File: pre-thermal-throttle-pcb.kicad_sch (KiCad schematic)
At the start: 21 parts, among them P1 Header 4, U1 CRE1S1205SC, U2 SN65HVD230, U3 MCP3008, U4 ESP32-DevKitC, U5 BMI088

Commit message: Label stuff
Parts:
- C1, C2: symbol pspice:CAP -> Device:C
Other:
- note added: "CAN"
- note added: "IMU"
- note added: "Steering Wheel + RS485 Transceiver"
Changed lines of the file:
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@@
   (junction (at 388.62 149.86) (diameter 0) (color 0 0 0 0)
   )
+  (wire (pts (xy 562.61 285.75) (xy 566.42 285.75))
+    (stroke (width 0) (type default) (color 0 0 0 0))
+  )
+  (polyline (pts (xy 345.44 87.63) (xy 490.22 87.63))
+    (stroke (width 0) (type default) (color 0 0 0 0))
+  )
   (wire (pts (xy 549.91 270.51) (xy 561.34 270.51))
     (stroke (width 0) (type default) (color 0 0 0 0))
   )
+  (wire (pts (xy 574.04 283.21) (xy 575.31 283.21))
+    (stroke (width 0) (type default) (color 0 0 0 0))
+  )
   (wire (pts (xy 549.91 283.21) (xy 557.53 283.21))
     (stroke (width 0) (type default) (color 0 0 0 0))
@@
     (stroke (width 0) (type default) (color 0 0 0 0))
   )
+  (polyline (pts (xy 345.44 87.63) (xy 345.44 175.26))
+    (stroke (width 0) (type default) (color 0 0 0 0))
+  )
   (wire (pts (xy 430.53 129.54) (xy 436.88 129.54))
     (stroke (width 0) (type default) (color 0 0 0 0))
@@
     (stroke (width 0) (type default) (color 0 0 0 0))
   )
+  (polyline (pts (xy 336.55 100.33) (xy 336.55 163.83))
+    (stroke (width 0) (type default) (color 0 0 0 0))
+  )
+  (polyline (pts (xy 233.68 100.33) (xy 233.68 163.83))
+    (stroke (width 0) (type default) (color 0 0 0 0))
+  )
+  (polyline (pts (xy 490.22 87.63) (xy 490.22 175.26))
+    (stroke (width 0) (type default) (color 0 0 0 0))
+  )
   (wire (pts (xy 514.35 288.29) (xy 511.81 288.29))
     (stroke (width 0) (type default) (color 0 0 0 0))
   )
+  (polyline (pts (xy 387.35 266.7) (xy 387.35 328.93))
+    (stroke (width 0) (type default) (color 0 0 0 0))
+  )
   (wire (pts (xy 252.73 213.36) (xy 252.73 215.9))
     (stroke (width 0) (type default) (color 0 0 0 0))
@@
     (stroke (width 0) (type default) (color 0 0 0 0))
   )
-  (wire (pts (xy 557.53 285.75) (xy 557.53 288.29))
+  (polyline (pts (xy 588.01 316.23) (xy 492.76 316.23))
+    (stroke (width 0) (type default) (color 0 0 0 0))
+  )
+  (wire (pts (xy 557.53 285.75) (xy 557.53 290.83))
     (stroke (width 0) (type default) (color 0 0 0 0))
   )
@@
     (stroke (width 0) (type default) (color 0 0 0 0))
   )
+  (polyline (pts (xy 292.1 266.7) (xy 387.35 266.7))
+    (stroke (width 0) (type default) (color 0 0 0 0))
+  )
+  (polyline (pts (xy 292.1 265.43) (xy 292.1 328.93))
+    (stroke (width 0) (type default) (color 0 0 0 0))
+  )
   (wire (pts (xy 317.5 294.64) (xy 307.34 294.64))
     (stroke (width 0) (type default) (color 0 0 0 0))
@@
     (stroke (width 0) (type default) (color 0 0 0 0))
   )
+  (polyline (pts (xy 588.01 252.73) (xy 588.01 316.23))
+    (stroke (width 0) (type default) (color 0 0 0 0))
+  )
   (wire (pts (xy 561.34 270.51) (xy 561.34 275.59))
     (stroke (width 0) (type default) (color 0 0 0 0))
@@
     (stroke (width 0) (type default) (color 0 0 0 0))
   )
+  (wire (pts (xy 561.34 275.59) (xy 563.88 275.59))
+    (stroke (width 0) (type default) (color 0 0 0 0))
+  )
   (wire (pts (xy 388.62 149.86) (xy 415.29 149.86))
     (stroke (width 0) (type default) (color 0 0 0 0))
@@
     (stroke (width 0) (type default) (color 0 0 0 0))
   )
+  (polyline (pts (xy 492.76 252.73) (xy 588.01 252.73))
+    (stroke (width 0) (type default) (color 0 0 0 0))
+  )
   (wire (pts (xy 551.18 278.13) (xy 551.18 280.67))
     (stroke (width 0) (type default) (color 0 0 0 0))
@@
     (stroke (width 0) (type default) (color 0 0 0 0))
   )
+  (wire (pts (xy 574.04 285.75) (xy 574.04 283.21))
+    (stroke (width 0) (type default) (color 0 0 0 0))
+  )
+  (polyline (pts (xy 233.68 100.33) (xy 336.55 100.33))
+    (stroke (width 0) (type default) (color 0 0 0 0))
+  )
   (wire (pts (xy 514.35 300.99) (xy 511.81 300.99))
     (stroke (width 0) (type default) (color 0 0 0 0))
@@
     (stroke (width 0) (type default) (color 0 0 0 0))
   )
+  (polyline (pts (xy 336.55 163.83) (xy 233.68 163.83))
+    (stroke (width 0) (type default) (color 0 0 0 0))
+  )
   (wire (pts (xy 368.3 149.86) (xy 368.3 132.08))
     (stroke (width 0) (type default) (color 0 0 0 0))
   )
+  (polyline (pts (xy 492.76 252.73) (xy 492.76 316.23))
+    (stroke (width 0) (type default) (color 0 0 0 0))
+  )
   (wire (pts (xy 345.44 299.72) (xy 345.44 302.26))
     (stroke (width 0) (type default) (color 0 0 0 0))
@@
     (stroke (width 0) (type default) (color 0 0 0 0))
   )
+  (wire (pts (xy 571.5 275.59) (xy 574.04 275.59))
+    (stroke (width 0) (type default) (color 0 0 0 0))
+  )
   (wire (pts (xy 363.22 149.86) (xy 368.3 149.86))
     (stroke (width 0) (type default) (color 0 0 0 0))
@@
     (stroke (width 0) (type default) (color 0 0 0 0))
   )
+  (polyline (pts (xy 490.22 175.26) (xy 345.44 175.26))
+    (stroke (width 0) (type default) (color 0 0 0 0))
+  )
   (wire (pts (xy 359.41 294.64) (xy 359.41 297.18))
     (stroke (width 0) (type default) (color 0 0 0 0))
@@
     (stroke (width 0) (type default) (color 0 0 0 0))
   )
-  (wire (pts (xy 562.61 278.13) (xy 562.61 283.21))
-    (stroke (width 0) (type default) (color 0 0 0 0))
+  (polyline (pts (xy 387.35 328.93) (xy 292.1 328.93))
+    (stroke (width 0) (type default) (color 0 0 0 0))
+  )
+  (wire (pts (xy 562.61 278.13) (xy 562.61 285.75))
+    (stroke (width 0) (type default) (color 0 0 0 0))
+  )
+  (text "IMU" (at 532.13 261.62 0)
+    (effects (font (size 3 3)) (justify left bottom))
   )
   (text "ADC" (at 444.5 114.3 0)
     (effects (font (size 5 5)) (justify left bottom))
   )
+  (text "Steering Wheel + RS485 Transceiver" (at 243.84 107.95 0)
+    (effects (font (size 3 3)) (justify left bottom))
+  )
   (text "some gpio pin" (at 474.98 220.98 0)
     (effects (font (size 1.27 1.27)) (justify left bottom))
+  )
+  (text "CAN" (at 330.2 278.13 0)
+    (effects (font (size 3 3)) (justify left bottom))
   )
   (text "Motor Thermistor Measurements" (at 351.79 97.79 0)
@@
     )
   )
-  (global_label "ESP MISO" (shape input) (at 557.53 288.29 0) (fields_autoplaced)
+  (global_label "ESP MISO" (shape input) (at 557.53 290.83 0) (fields_autoplaced)
     (effects (font (size 1.27 1.27)) (justify left))
-    (property "Intersheet References" "${INTERSHEET_REFS}" (id 0) (at 569.1355 288.2106 0)
+    (property "Intersheet References" "${INTERSHEET_REFS}" (id 0) (at 569.1355 290.7506 0)
       (effects (font (size 1.27 1.27)) (justify left) hide)
     )
@@
     (pin "2")
   )
-  (symbol (lib_id "pspice:CAP") (at 568.96 283.21 90) (unit 1)
-    (in_bom yes) (on_board yes) (fields_autoplaced)
-    (property "Reference" "C2" (id 0) (at 568.96 274.32 90))
-    (property "Value" "100 nF" (id 1) (at 568.96 276.86 90))
-    (property "Footprint" "" (id 2) (at 568.96 283.21 0)
-      (effects (font (size 1.27 1.27)) hide)
-    )
-    (property "Datasheet" "~" (id 3) (at 568.96 283.21 0)
+  (symbol (lib_id "Device:C") (at 570.23 285.75 90) (unit 1)
+    (in_bom yes) (on_board yes)
+    (property "Reference" "C2" (id 0) (at 570.23 279.4 90))
+    (property "Value" "100 nF" (id 1) (at 570.23 281.94 90))
+    (property "Footprint" "" (id 2) (at 574.04 284.7848 0)
+      (effects (font (size 1.27 1.27)) hide)
+    )
+    (property "Datasheet" "~" (id 3) (at 570.23 285.75 0)
       (effects (font (size 1.27 1.27)) hide)
     )
@@
     (pin "1")
   )
-  (symbol (lib_id "pspice:CAP") (at 567.69 275.59 90) (unit 1)
-    (in_bom yes) (on_board yes) (fields_autoplaced)
-    (property "Reference" "C1" (id 0) (at 567.69 266.7 90))
-    (property "Value" "100 nF" (id 1) (at 567.69 269.24 90))
-    (property "Footprint" "" (id 2) (at 567.69 275.59 0)
-      (effects (font (size 1.27 1.27)) hide)
-    )
+  (symbol (lib_id "Device:C") (at 567.69 275.59 90) (unit 1)
+    (in_bom yes) (on_board yes)
+    (property "Reference" "C1" (id 0) (at 567.69 269.24 90))
+    (property "Value" "100 nF" (id 1) (at 567.69 271.78 90))
+    (property "Footprint" "" (id 2) (at 571.5 274.6248 0)
+      (effects (font (size 1.27 1.27)) hide)
+    )

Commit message: Add switching regulator circuit basic schematic, values need compute
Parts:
- removed P1: Header 4, symbol Connector:Conn_01x04_Female
- removed U1: CRE1S1205SC, Converter_DCDC:Converter_DCDC_Murata_CRE1xxxxxxSC_THT, symbol Regulator_Switching:CRE1S1205SC
- added CREG3, CREG5, CREGin: C, symbol Device:C
- added CREGout: C_Polarized, symbol Device:C_Polarized
- added DREG1: D, symbol Device:D
- added IC1: A7986ATR, SOIC127P600X175-9N, symbol A7986ATR:A7986ATR
- added J2: Motor Throttle Connector, Connector_JST:JST_PH_B2B-PH-K_1x02_P2.00mm_Vertical, symbol Connector:Conn_01x02_Female
- added LREG1: L, symbol Device:L
- added R7: 1M, Resistor_SMD:R_0805_2012Metric, symbol Device:R
- added RREG1, RREG2, RREG3: R, symbol Device:R
- gave numbers to parts that had none: 10
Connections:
- net ESP MISO is gone; now on net ESP CIPO: U5.10 (SDO2), U5.15 (SDO1)
- net ESP MOSI is gone; now on net ESP COPI: U5.9 (SDA/SDI)
- net +12V: now also CREGin.1, IC1.3 (EN), IC1.8 (VCC)
- net +3.3V: now also U2.3 (VCC), U3.16 (Vdd), U4.1 (3V3), CREGout.1, LREG1.2, RREG1.2
- net +5V: now also U3.15 (Vref), U4.19 (5V)
- net ESP Accel : now also U4.33 (GPIO21)
- net ESP Gyro CS: now also U4.36 (GPIO22)
- net ESP SPI CLK: now also U3.13 (CLK), U4.30 (GPIO18)
- net GND: now also U2.2 (GND), U3.14 (AGND), U3.9 (DGND), U4.14 (GND), U4.32 (GND), U4.38 (GND), CREGin.2, CREGout.2, DREG1.2 (A), IC1.7 (GND), J2.2 (Pin_2), R7.2, RREG2.1
- net CAN_RXD: now reaches U4.10 (DAC_2/ADC2_CH9/GPIO26)
- net CAN_RXD: now also U2.4 (R)
- net ESP CIPO: now reaches U4.31 (GPIO19)
- net ESP CIPO: now also U3.12 (Dout)
- net ESP COPI: now reaches U4.37 (GPIO23)
- net ESP COPI: now also U3.11 (Din)
- net ESP ADC CS: now reaches U4.4 (SENSOR_VN/GPIO39/ADC1_CH3)
- net ESP ADC CS: now also U3.10 (~{CS}/SHDN)
- net CAN_TXD: now reaches U4.9 (DAC_1/ADC2_CH8/GPIO25)
- net CAN_TXD: now also U2.1 (D)
- net at R1.1, U2.8 (Rs): no longer U2.2 (GND)
- net THROTTLE_SIG: now reaches U3.5 (CH4)
- net THROTTLE_SIG: now also J2.1 (Pin_1), R7.1
- new net: CREG3.1, RREG3.2
- new net: CREG3.2, CREG5.1, IC1.5 (FB), RREG1.1, RREG2.2
- new net: CREG5.2, IC1.4 (COMP), RREG3.1
- new net: DREG1.1 (K), IC1.1 (OUT), LREG1.1
- no-connect marks 0 -> 4
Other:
- note added: "12V-3.3V Switching Regulator"
- note added: "5V Reference (For thermistor ONLY)"
- moved on the sheet: C1, C2, U5

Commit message: Setup footprints and add bypass caps
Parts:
- removed can1: Header 2, symbol Connector:Conn_01x02_Female
- added C1, C10, C11, C12, C13, C2, C3, C4, C5, C8, C9: 100 nF, Capacitor_SMD:C_0805_2012Metric, symbol Device:C
- added J1: RJHSE-5381-ND, Connector_RJ:RJ45_Amphenol_RJHSE538X, symbol Connector:RJ45_LED_Shielded
- added R3, R5: 130R, Resistor_SMD:R_0805_2012Metric, symbol Device:R_US
- added R4: 10K, Resistor_SMD:R_0805_2012Metric, symbol Device:R_US
- added R6: 120R, Resistor_THT:R_Axial_DIN0309_L9.0mm_D3.2mm_P15.24mm_Horizontal, symbol Device:R_US
- C6: renamed from C1; footprint (none) -> Capacitor_SMD:C_0805_2012Metric
- C7: renamed from C2; footprint (none) -> Capacitor_SMD:C_0805_2012Metric
- CREG3, CREG5: footprint (none) -> Capacitor_SMD:C_0805_2012Metric
- CREGin1: renamed from CREGin; footprint (none) -> Capacitor_SMD:C_0805_2012Metric
- CREGout1: renamed from CREGout; footprint (none) -> Capacitor_THT:CP_Radial_D8.0mm_P3.80mm
- DREG1: footprint (none) -> Diode_SMD:D_0805_2012Metric
- LREG1: footprint (none) -> Inductor_SMD:L_Taiyo-Yuden_NR-80xx_HandSoldering
- R1, RREG1, RREG2, RREG3: footprint (none) -> Resistor_SMD:R_0805_2012Metric
- R2: value 120 -> 120R; footprint (none) -> Resistor_THT:R_Axial_DIN0309_L9.0mm_D3.2mm_P15.24mm_Horizontal
- TH1, TH2, TH3, TH4: footprint (none) -> Connector_JST:JST_PH_B2B-PH-K_1x02_P2.00mm_Vertical
- U3: renamed from U6; value MAX3485 -> MAX3485CSA; footprint (none) -> Package_SO:SOIC-8-1EP_3.9x4.9mm_P1.27mm_EP2.41x3.81mm_ThermalVias
- U4: renamed from U3; footprint (none) -> Package_DIP:DIP-16_W7.62mm
- renumbered J1 to J2, J2 to J3, R6 to R10, R7 to R11, R3 to R7, R4 to R8, R5 to R9, U2 to U1, U5 to U2, U4 to U5
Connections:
- net +12V: now also C4.1, C5.1, J1.4, J1.5
- net +3.3V: now also C1.1, C11.1, C13.1, C3.2, J1.12
- net +5V: now also C10.1, C12.1, C8.1, C9.1
- net GND: now also C1.2, C10.2, C11.2, C12.2, C13.2, C2.1, C3.1, C4.2, C5.2, C8.2, C9.2, J1.7, J1.8, R3.1, R4.2, R5.1
- net RS485 RTS: now also U5.5 (VDET_1/GPIO34/ADC1_CH6)
- net STEERING_A: now also R6.2
- net STEERING_B: now also R6.1
- net CAR_CANH: now reaches R2.1, U1.7 (CANH)
- net CAR_CANH: now also J1.1
- net CAR_CANL: now reaches R2.2, U1.6 (CANL)
- net CAR_CANL: now also J1.2
- net ESP_OK_LED: now reaches U5.3 (SENSOR_VP/GPIO36/ADC1_CH0)
- net ESP_OK_LED: now also C2.2, J1.10, R4.1
- new net: J1.11, R3.2
- new net: J1.9, R5.2
- no-connect marks 4 -> 5
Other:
- note added: "Car-wide connection"
- note added: "GREEN"
- note added: "Power layout follows POE standard mode B LEDs are yellow, green at 2V, 10mA"
- note added: "YELLOW"
- note removed: "some gpio pin"
- moved on the sheet: C6, C7, CREG3, CREG5, CREGin1, CREGout1, DREG1, IC1, J2, J3, LREG1, R1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

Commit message: Finish part selection
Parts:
- removed CREG3, CREG5: C, Capacitor_SMD:C_0805_2012Metric, symbol Device:C
- removed CREGout1: C_Polarized, Capacitor_THT:CP_Radial_D8.0mm_P3.80mm, symbol Device:C_Polarized
- removed DREG1: D, Diode_SMD:D_0805_2012Metric, symbol Device:D
- removed IC1: A7986ATR, SOIC127P600X175-9N, symbol A7986ATR:A7986ATR
- removed RREG1, RREG2, RREG3: R, Resistor_SMD:R_0805_2012Metric, symbol Device:R
- added C14, C15, C16, C17, C18, C19, C20, C21: 100 nF, Capacitor_SMD:C_0805_2012Metric, symbol Device:C
- added CREGboot1, CREGinx1: 100nF, Capacitor_SMD:C_0805_2012Metric, symbol Device:C
- added CREGin2, CREGin3: 1uF, Capacitor_SMD:C_0805_2012Metric, symbol Device:C
- added CREGout1: 47uF, Capacitor_SMD:C_0805_2012Metric, symbol Device:C
- added H1, H2, H3, H4: MountingHole_Pad, MountingHole:MountingHole_3mm_Pad_Via, symbol Mechanical:MountingHole_Pad
- added IC1: LMR51420XFDDCR, SOT95P280X110-6N, symbol LMR51420XFDDCR:LMR51420XFDDCR
- added IC2, IC3, IC4, IC5: ADR02BRZ-REEL7, ADR02BRZ:SOIC127P600X175-8N, symbol ADR02BRZ-REEL7:ADR02BRZ-REEL7
- added RREGfbb1: 22.1k, Resistor_SMD:R_0805_2012Metric, symbol Device:R_US
- added RREGfbt1: 100k, Resistor_SMD:R_0805_2012Metric, symbol Device:R_US
- CREGin1: value C -> 1uF
- J2: footprint Connector_JST:JST_PH_B4B-PH-K_1x04_P2.00mm_Vertical -> Connector_JST:JST_XH_B4B-XH-A_1x04_P2.50mm_Vertical
- J3, TH1, TH2, TH3, TH4: footprint Connector_JST:JST_PH_B2B-PH-K_1x02_P2.00mm_Vertical -> Connector_JST:JST_XH_B2B-XH-A_1x02_P2.50mm_Vertical
- LREG1: value L -> 6uH SRP1265A-6R0M; footprint Inductor_SMD:L_Taiyo-Yuden_NR-80xx_HandSoldering -> libraries:L_Bourns_SRP1260A
- U2: footprint PQFN50P450X300X100-16N -> bmi088:PQFN50P450X300X100-16N
- U3: footprint Package_SO:SOIC-8-1EP_3.9x4.9mm_P1.27mm_EP2.41x3.81mm_ThermalVias -> libraries:SOIC-8-1EP_3.9x4.9mm_P1.27mm_EP2.41x3.81mm_ThermalVias
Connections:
- net +12V: now also C14.2, C15.2, C16.2, C17.2, CREGin2.1, CREGin3.1, CREGinx1.1, IC1.3 (VIN), IC1.5 (EN), IC2.2 (VIN), IC3.2 (VIN), IC4.2 (VIN), IC5.2 (VIN)
- net +3.3V: now also CREGout1.1, RREGfbt1.1
- net +5V: no longer TH1.1, TH2.1, TH3.1, TH4.1
- net GND: now also C14.1, C15.1, C16.1, C17.1, C18.1, C19.1, C20.1, C21.1, CREGin2.2, CREGin3.2, CREGinx1.2, CREGout1.2, H1.1, H2.1, H3.1, H4.1, IC1.1 (GND), IC2.4 (GND), IC3.4 (GND), IC4.4 (GND), IC5.4 (GND), RREGfbb1.2
- net ADC_CH0: now reaches R7.1, U4.1 (CH0)
- net ADC_CH0: now also TH1.1; no longer TH1.2
- net ADC_CH2: now reaches R8.1, U4.3 (CH2)
- net ADC_CH2: now also TH2.1; no longer TH2.2
- net ADC_CH1: now reaches R9.1, U4.2 (CH1)
- net ADC_CH1: now also TH3.1; no longer TH3.2
- net at LREG1.1: now also CREGboot1.2, IC1.2 (SW)
- new net: CREGboot1.1, IC1.6 (CB)
- new net: C18.2, IC2.6 (VOUT), TH1.2
- new net: C21.2, IC5.6 (VOUT), TH4.2
- new net: C20.2, IC4.6 (VOUT), TH3.2
- new net: IC1.4 (FB), RREGfbb1.1, RREGfbt1.2
- new net: C19.2, IC3.6 (VOUT), TH2.2
- new net ADC_CH3: U4.4 (CH3)
- new net ADC_CH4: R10.1, TH4.1
- no-connect marks 5 -> 22
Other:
- note added: "ESP32"
- note removed: "5V Reference (For thermistor ONLY)"
- moved on the sheet: C10, C11, C12, C13, C2, C3, C4, C5, C6, C7, C8, C9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

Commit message: Add extra rj45 for CAN splice and connect imu ints
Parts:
- added C22, C23, C24, C25: 100 nF, Capacitor_SMD:C_0805_2012Metric, symbol Device:C
- added J4: RJHSE-5381-ND, Connector_RJ:RJ45_Amphenol_RJHSE538X, symbol Connector:RJ45_LED_Shielded
- added R12, R14: 130R, Resistor_SMD:R_0805_2012Metric, symbol Device:R_US
- added R13: 10K, Resistor_SMD:R_0805_2012Metric, symbol Device:R_US
- IC1: footprint SOT95P280X110-6N -> LMR51420XFDDCR:SOT95P280X110-6N
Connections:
- net +12V: now also C24.1, C25.1, J4.4, J4.5
- net +3.3V: now also C23.2, J4.12
- net CAR_CANH: now also J4.1
- net CAR_CANL: now also J4.2
- net ESP_OK_LED: now also C22.2, J4.10, R13.1
- net GND: now also C22.1, C23.1, C24.2, C25.2, J4.7, J4.8, R12.1, R13.2, R14.1
- net IMU_INT1: now reaches U5.21 (SD_DATA0/GPIO7)
- net IMU_INT1: now also U2.16 (INT1)
- net IMU_INT2: now reaches U5.22 (SD_DATA1/GPIO8)
- net IMU_INT2: now also U2.13 (INT4)
- new net: J4.11, R12.2
- new net: J4.9, R14.2
- no-connect marks 22 -> 23

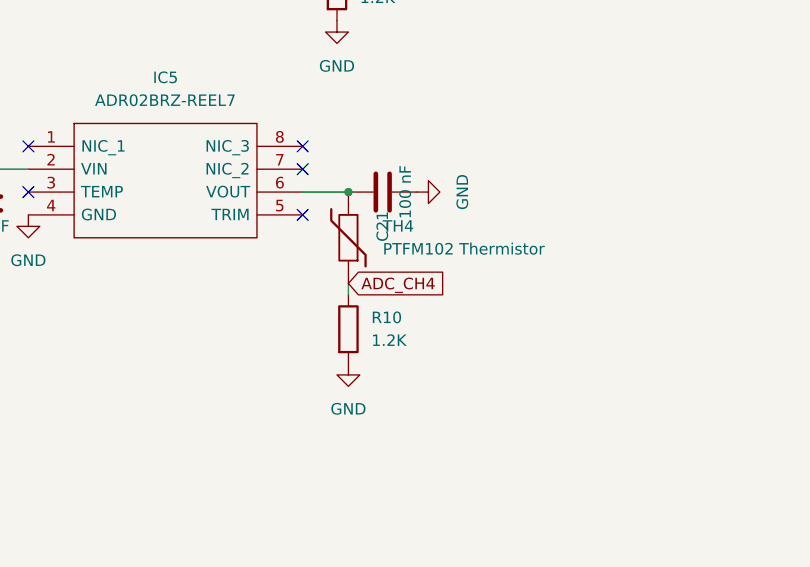
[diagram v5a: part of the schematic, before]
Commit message: Finish most traces
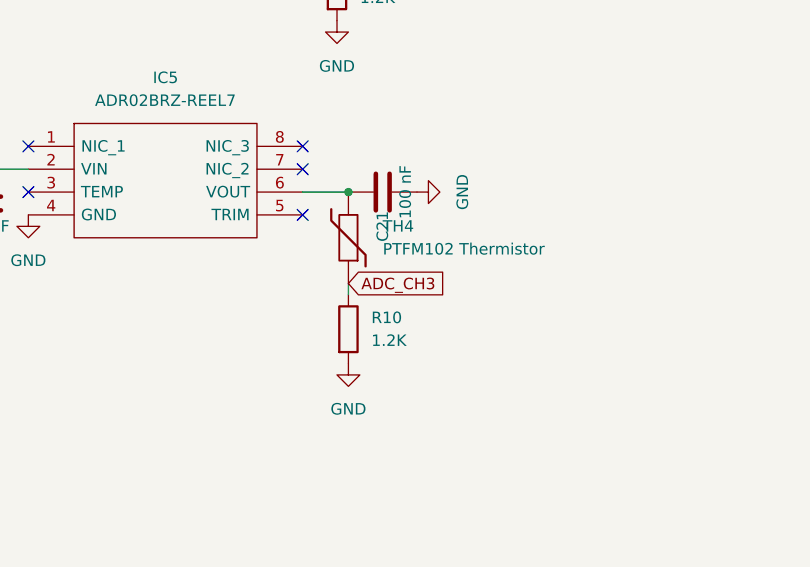
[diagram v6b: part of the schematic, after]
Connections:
- net ADC_CH4 is gone; now on net ADC_CH3: R10.1, TH4.1
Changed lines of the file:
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@@
     )
   )
-  (global_label "ADC_CH4" (shape input) (at 270.51 358.14 0) (fields_autoplaced)
+  (global_label "ADC_CH3" (shape input) (at 270.51 358.14 0) (fields_autoplaced)
     (effects (font (size 1.27 1.27)) (justify left))
     (property "Intersheet References" "${INTERSHEET_REFS}" (id 0) (at 281.3293 358.0606 0)
